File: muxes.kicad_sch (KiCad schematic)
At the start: 11 parts, among them J1 JST_SH_BM10B-SRSS-TB_1x10-1MP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, J2 JST_SH_BM10B-SRSS-TB_1x10-1MP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, J3 JST_SH_BM10B-SRSS-TB_1x10-1MP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, J4 JST_SH_BM10B-SRSS-TB_1x10-1MP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, J5 JST_SH_BM10B-SRSS-TB_1x10-1MP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, J6 JST_SH_BM10B-SRSS-TB_1x10-1MP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, J7 JST_SH_BM12B-SRSS-TB_1x12-1MP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

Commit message: Update
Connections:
- net +3.3V renamed +3.3V_SYS
- net +5V renamed +5V_SYS
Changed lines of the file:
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@@
 		(on_board yes)
 		(dnp no)
-		(fields_autoplaced yes)
 		(property "Reference" "#PWR06"
 			(at 115.57 60.96 0)
@@
 			)
 		)
-		(property "Value" "+3.3V"
-			(at 107.95 60.9599 90)
+		(property "Value" "+3.3V_SYS"
+			(at 103.124 60.96 90)
 			(effects
 				(font
 					(size 1.27 1.27)
 				)
-				(justify left)
 			)
 		)
@@
 		(on_board yes)
 		(dnp no)
-		(fields_autoplaced yes)
 		(property "Reference" "#PWR09"
 			(at 171.45 60.96 0)
@@
 			)
 		)
-		(property "Value" "+3.3V"
-			(at 163.83 60.9599 90)
+		(property "Value" "+3.3V_SYS"
+			(at 157.988 61.214 90)
 			(effects
 				(font
 					(size 1.27 1.27)
 				)
-				(justify left)
 			)
 		)
@@
 		(on_board yes)
 		(dnp no)
-		(fields_autoplaced yes)
 		(property "Reference" "#PWR028"
 			(at 208.28 119.38 0)
@@
 			)
 		)
-		(property "Value" "+5V"
-			(at 200.66 119.3799 90)
+		(property "Value" "+5V_SYS"
+			(at 196.85 119.38 90)
 			(effects
 				(font
 					(size 1.27 1.27)
 				)
-				(justify left)
 			)
 		)
@@
 		(on_board yes)
 		(dnp no)
-		(fields_autoplaced yes)
 		(property "Reference" "#PWR016"
 			(at 81.28 119.38 0)
@@
 			)
 		)
-		(property "Value" "+5V"
-			(at 73.66 119.3799 90)
+		(property "Value" "+5V_SYS"
+			(at 69.85 119.126 90)
 			(effects
 				(font
 					(size 1.27 1.27)
 				)
-				(justify left)
 			)
 		)
@@
 		(on_board yes)
 		(dnp no)
-		(fields_autoplaced yes)
 		(property "Reference" "#PWR026"
 			(at 176.53 121.92 0)
@@
 			)
 		)
-		(property "Value" "+3.3V"
-			(at 168.91 121.9199 90)
+		(property "Value" "+3.3V_SYS"
+			(at 164.084 122.174 90)
 			(effects
 				(font
 					(size 1.27 1.27)
 				)
-				(justify left)
 			)
 		)
@@
 		(on_board yes)
 		(dnp no)
-		(fields_autoplaced yes)
 		(property "Reference" "#PWR029"
 			(at 208.28 121.92 0)
@@
 			)
 		)
-		(property "Value" "+3.3V"
-			(at 200.66 121.9199 90)
+		(property "Value" "+3.3V_SYS"
+			(at 195.834 122.174 90)
 			(effects
 				(font
 					(size 1.27 1.27)
 				)
-				(justify left)
 			)
 		)
@@
 		(on_board yes)
 		(dnp no)
-		(fields_autoplaced yes)
 		(property "Reference" "#PWR014"
 			(at 49.53 121.92 0)
@@
 			)
 		)
-		(property "Value" "+3.3V"
-			(at 41.91 121.9199 90)
+		(property "Value" "+3.3V_SYS"
+			(at 36.068 122.428 90)
 			(effects
 				(font
 					(size 1.27 1.27)
 				)
-				(justify left)
 			)
 		)
@@
 		(on_board yes)
 		(dnp no)
-		(fields_autoplaced yes)
 		(property "Reference" "#PWR012"
 			(at 231.14 60.96 0)
@@
 			)
 		)
-		(property "Value" "+3.3V"
-			(at 223.52 60.9599 90)
+		(property "Value" "+3.3V_SYS"
+			(at 218.948 60.96 90)
 			(effects
 				(font
 					(size 1.27 1.27)
 				)
-				(justify left)
 			)
 		)
@@
 		(on_board yes)
 		(dnp no)
-		(fields_autoplaced yes)
 		(property "Reference" "#PWR023"
 			(at 144.78 121.92 0)
@@
 			)
 		)
-		(property "Value" "+3.3V"
-			(at 137.16 121.9199 90)
+		(property "Value" "+3.3V_SYS"
+			(at 132.334 121.92 90)
 			(effects
 				(font
 					(size 1.27 1.27)
 				)
-				(justify left)
 			)
 		)
@@
 		(on_board yes)
 		(dnp no)
-		(fields_autoplaced yes)
 		(property "Reference" "#PWR015"
 			(at 49.53 119.38 0)
@@
 			)
 		)
-		(property "Value" "+5V"
-			(at 41.91 119.3799 90)
+		(property "Value" "+5V_SYS"
+			(at 36.322 119.126 90)
 			(effects
 				(font
 					(size 1.27 1.27)
 				)
-				(justify left)
 			)
 		)
@@
 		(on_board yes)
 		(dnp no)
-		(fields_autoplaced yes)
 		(property "Reference" "#PWR022"
 			(at 144.78 119.38 0)
@@
 			)
 		)
-		(property "Value" "+5V"
-			(at 137.16 119.3799 90)
+		(property "Value" "+5V_SYS"
+			(at 133.35 119.38 90)
 			(effects
 				(font
 					(size 1.27 1.27)
 				)
-				(justify left)
 			)
 		)
@@
 		(on_board yes)
 		(dnp no)
-		(fields_autoplaced yes)
 		(property "Reference" "#PWR019"
 			(at 113.03 119.38 0)
@@
 			)
 		)
-		(property "Value" "+5V"
-			(at 105.41 119.3799 90)
+		(property "Value" "+5V_SYS"
+			(at 101.6 119.126 90)
 			(effects
 				(font
 					(size 1.27 1.27)
 				)
-				(justify left)
 			)
 		)
@@
 		(on_board yes)
 		(dnp no)
-		(fields_autoplaced yes)
 		(property "Reference" "#PWR025"
 			(at 176.53 119.38 0)
@@
 			)
 		)
-		(property "Value" "+5V"
-			(at 168.91 119.3799 90)
+		(property "Value" "+5V_SYS"
+			(at 164.846 119.38 90)
 			(effects
 				(font
 					(size 1.27 1.27)
 				)
-				(justify left)
 			)
 		)
@@
 		(on_board yes)
 		(dnp no)
-		(fields_autoplaced yes)
 		(property "Reference" "#PWR017"
 			(at 81.28 121.92 0)
@@
 			)
 		)
-		(property "Value" "+3.3V"
-			(at 73.66 121.9199 90)
+		(property "Value" "+3.3V_SYS"
+			(at 68.834 122.174 90)
 			(effects
 				(font
 					(size 1.27 1.27)
 				)
-				(justify left)
 			)
 		)
@@
 		(on_board yes)
 		(dnp no)
-		(fields_autoplaced yes)
 		(property "Reference" "#PWR03"
 			(at 60.96 60.96 0)
@@
 			)
 		)
-		(property "Value" "+3.3V"
-			(at 53.34 60.9599 90)
+		(property "Value" "+3.3V_SYS"
+			(at 47.752 60.96 90)
 			(effects
 				(font
 					(size 1.27 1.27)
 				)
-				(justify left)
 			)
 		)
@@
 		(on_board yes)
 		(dnp no)
-		(fields_autoplaced yes)
 		(property "Reference" "#PWR031"
 			(at 240.03 121.92 0)
@@
 			)
 		)
-		(property "Value" "+5V"
-			(at 232.41 121.9199 90)
+		(property "Value" "+5V_SYS"
+			(at 228.6 121.92 90)
 			(effects
 				(font
 					(size 1.27 1.27)
 				)
-				(justify left)
 			)
 		)
@@
 		(on_board yes)
 		(dnp no)
-		(fields_autoplaced yes)
 		(property "Reference" "#PWR020"
 			(at 113.03 121.92 0)
@@
 			)
 		)
-		(property "Value" "+3.3V"
-			(at 105.41 121.9199 90)
+		(property "Value" "+3.3V_SYS"
+			(at 100.584 122.174 90)
 			(effects
 				(font
 					(size 1.27 1.27)
 				)
-				(justify left)
 			)
 		)
@@
 		(on_board yes)
 		(dnp no)
-		(fields_autoplaced yes)
 		(property "Reference" "#PWR032"
 			(at 240.03 124.46 0)
@@
 			)
 		)
-		(property "Value" "+3.3V"
-			(at 232.41 124.4599 90)
+		(property "Value" "+3.3V_SYS"
+			(at 227.838 124.714 90)
 			(effects
 				(font
 					(size 1.27 1.27)
 				)
-				(justify left)
 			)
 		)

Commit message: Fix global nets
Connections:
- net MUX2_D: no longer S2.13 (D)

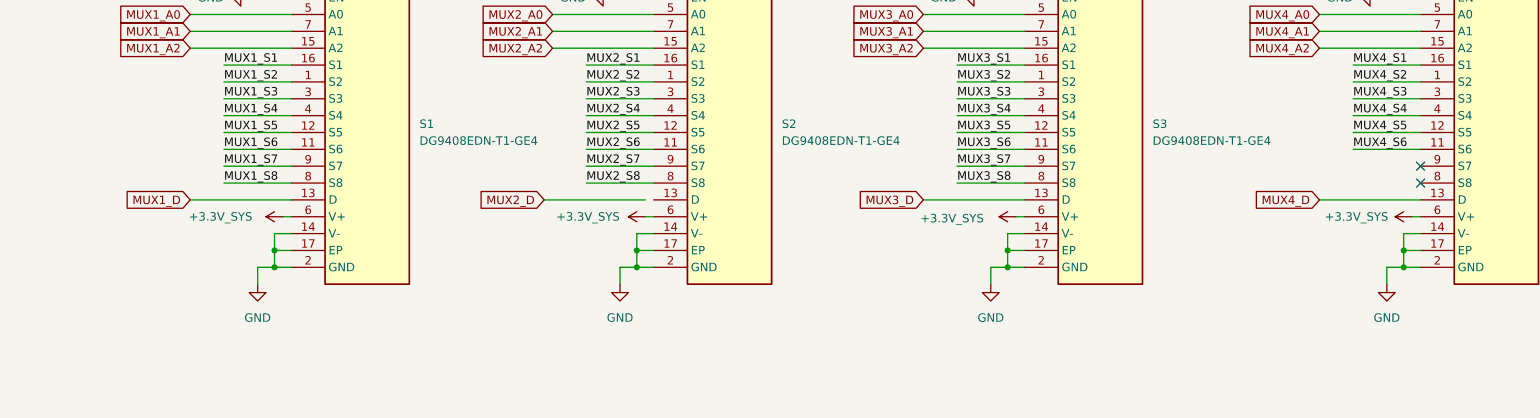
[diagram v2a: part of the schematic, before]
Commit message: Trace the board
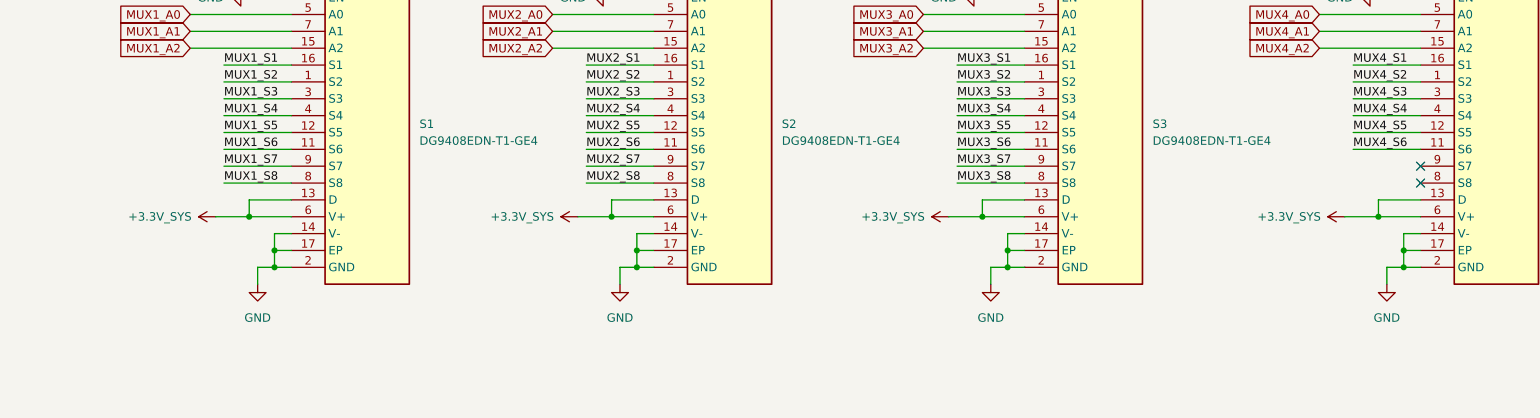
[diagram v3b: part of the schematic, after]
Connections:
- net +3.3V_SYS: now also S1.13 (D), S2.13 (D), S3.13 (D), S4.13 (D)
- net MUX1_D: no longer S1.13 (D)
- net MUX3_D: no longer S3.13 (D)
- net MUX4_D: no longer S4.13 (D)
